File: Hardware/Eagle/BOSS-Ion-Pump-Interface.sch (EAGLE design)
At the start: 38 parts, among them J1 MOLEX-22112022, J2 MOLEX-22112042, J3 MOLEX-22112042, J4 MOLEX-22112062, SW1 SPST-OFFBOARD, SW2 SPST-OFFBOARD, U1 ISO224ADWVR, U2 ISO224ADWVR

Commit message: Re-labeled nets, added 10uF filter on+5V in
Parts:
- added C15: 10uF 50V, AUmlib:C-USC1210
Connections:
- net +15V-BLUE renamed +15V-A
- net +15V-RED renamed +15V-B
- net +VIN-BLUE renamed +VIN-A
- net +VIN-RED renamed +VIN-B
- net FROM-BLUE-PUMP renamed FROM-PUMP-A
- net FROM-RED-PUMP renamed FROM-PUMP-B
- net GND-ISO-BLUE renamed GND-ISO-A
- net GND-ISO-RED renamed GND-ISO-B
- net IN-BLUE renamed IN-A
- net IN-RED renamed IN-B
- net VCAP-BLUE renamed VCAP-A
- net VCAP-RED renamed VCAP-B
- net VDD1-BLUE renamed VDD1-A
- net VDD1-RED renamed VDD1-B
- removed net OUTN-BLUE: J4.5, TVS3.C2, U$11.5, U2.OUTN
- removed net OUTN-RED: J4.4, TVS3.C3, U$11.4, U1.OUTN
- removed net OUTP-BLUE: J4.6, TVS3.C1, U$11.6, U2.OUTP
- removed net OUTP-RED: J4.3, TVS3.C4, U$11.3, U1.OUTP
- new net OUTN-A: J4.5, TVS3.C2, U$11.4, U$11.5, U2.OUTN
- new net OUTN-B: J4.4, TVS3.C3, U1.OUTN
- new net OUTP-A: J4.6, TVS3.C1, U$11.3, U$11.6, U2.OUTP
- new net OUTP-B: J4.3, TVS3.C4, U1.OUTP
- net +5V: now also C15.1
- net GND: now also C15.2
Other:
- moved on the sheet: C4, R2

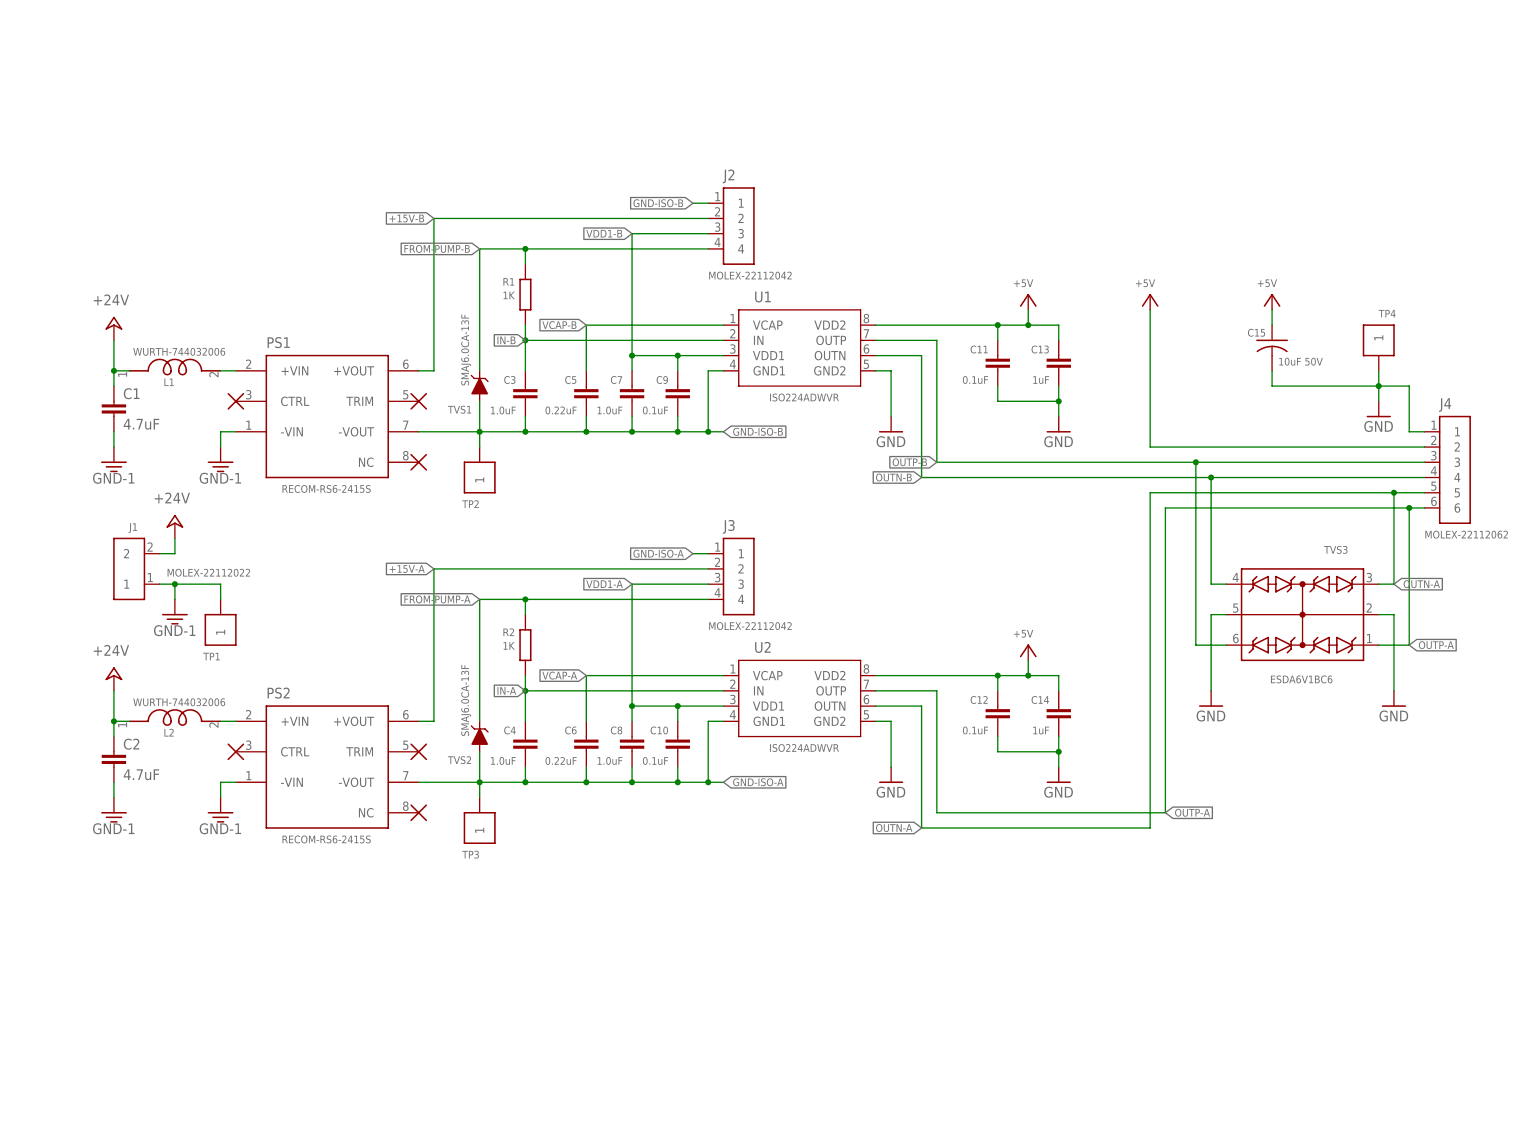
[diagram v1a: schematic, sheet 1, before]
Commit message: Added reverse polarity protection
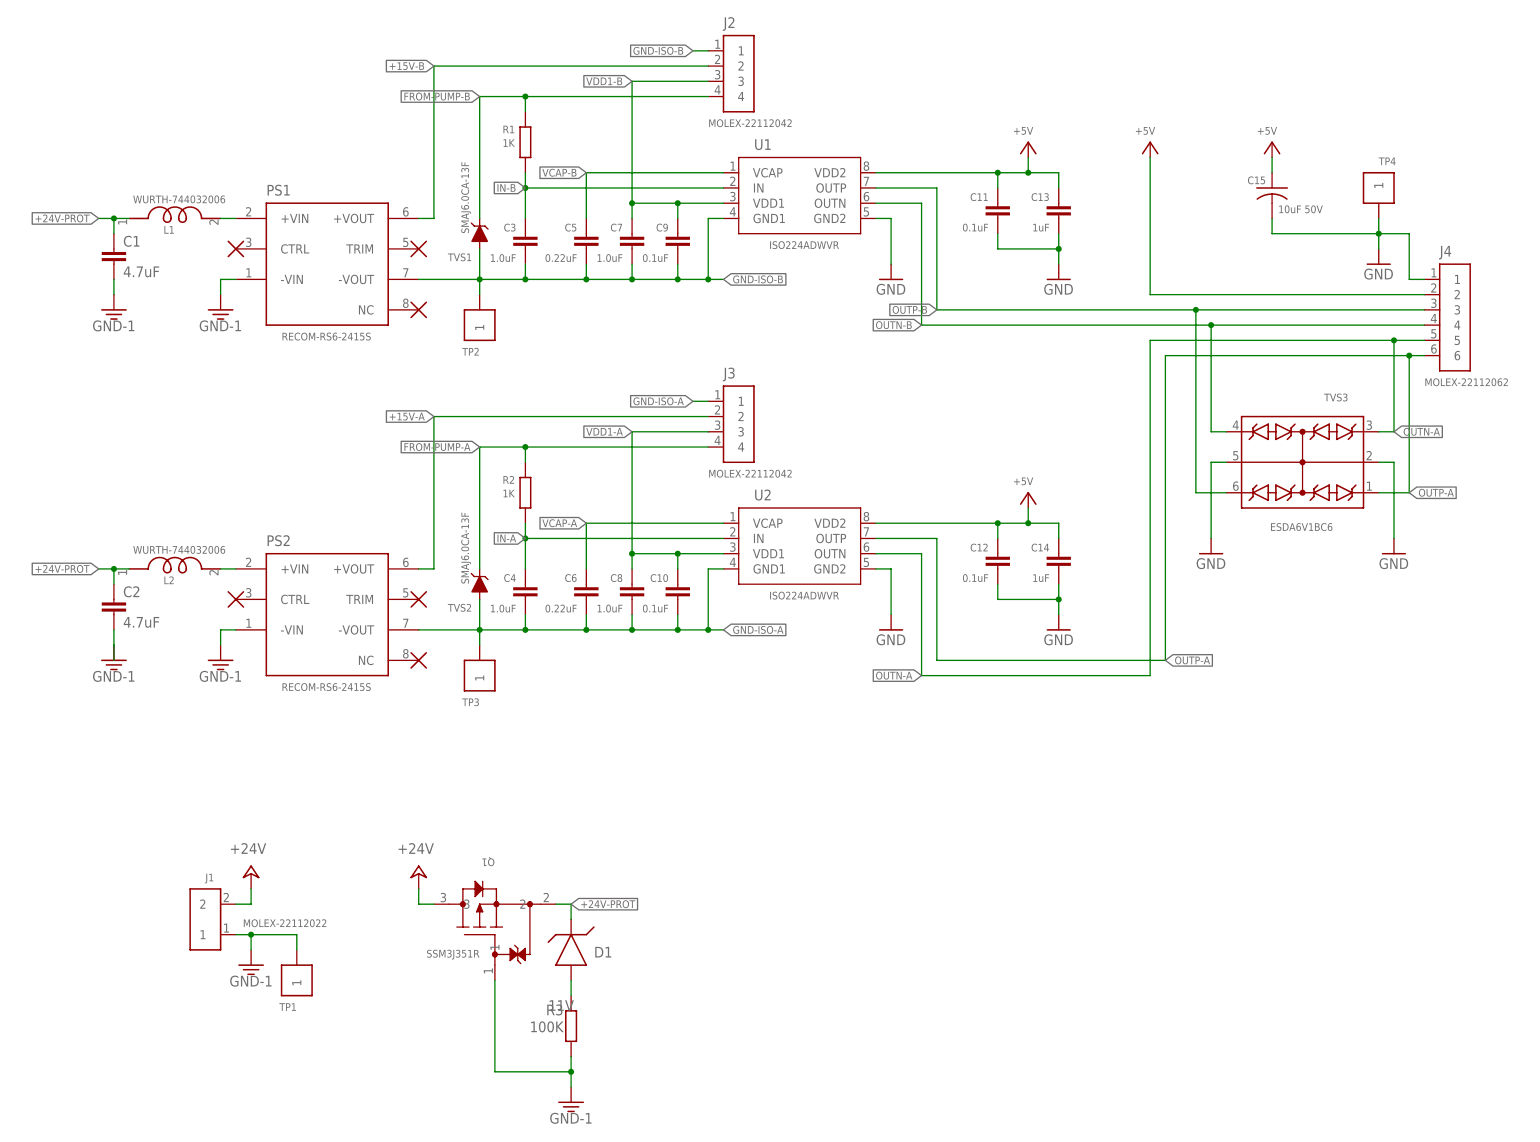
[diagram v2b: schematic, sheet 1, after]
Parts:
- added D1: 11V, AUmlib:ZENER-BZT52C11-7-F
- added Q1: SSM3J351R, AUmlib:P-MOSFET-SSM3J351R
- added R3: 100K, AUmlib:R-EU_R0805
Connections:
- new net +24V-PROT: C1.1, C2.1, D1.C, L1.1, L2.1, Q1.2
- new net N$2: D1.A, R3.2
- net +24V: now also Q1.3; no longer C1.1, C2.1, L1.1, L2.1
- net GND-1: now also Q1.1, R3.1
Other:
- moved on the sheet: C1, C10, C11, C12, C13, C14, C15, C2, C3, C4, C5, C6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

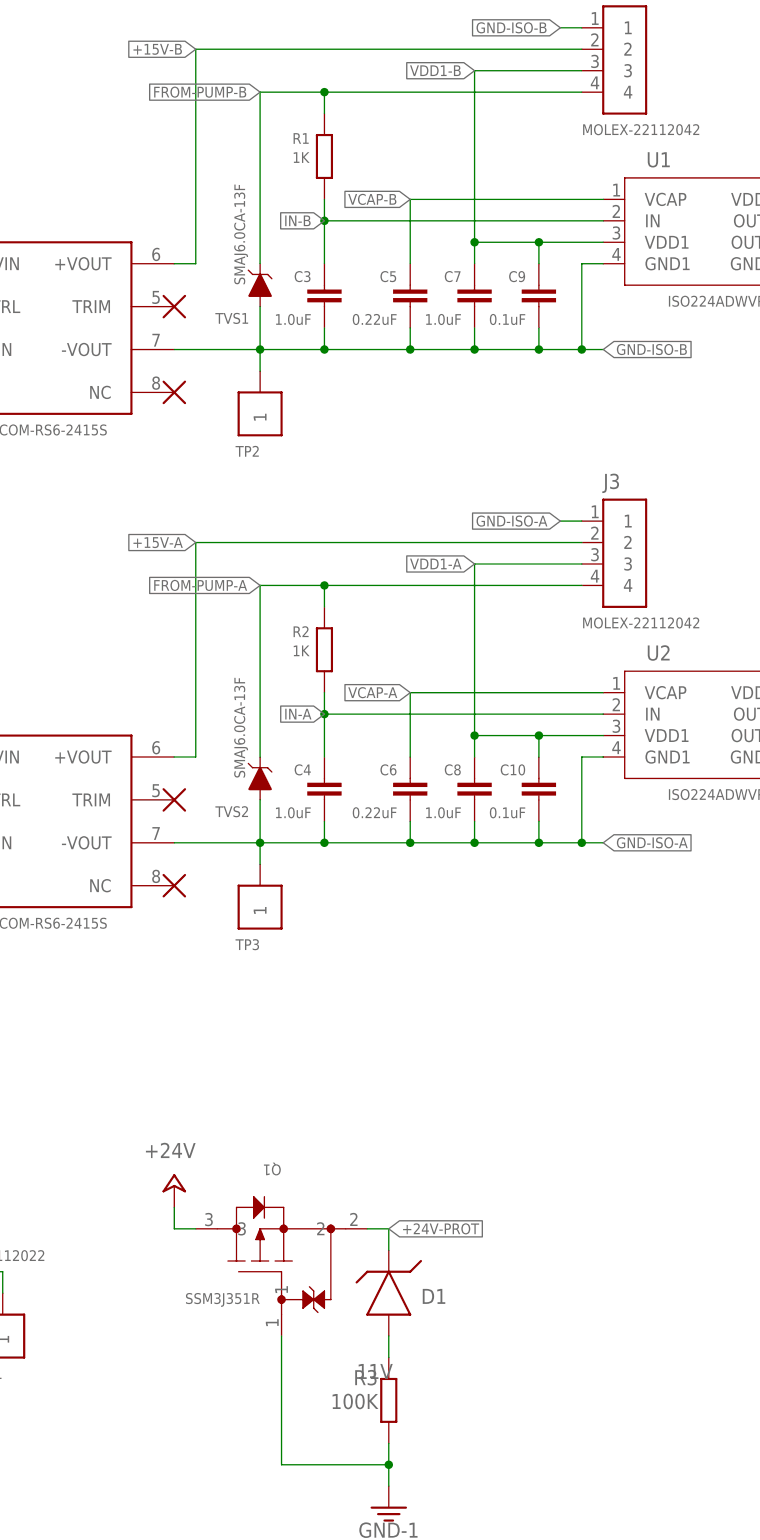
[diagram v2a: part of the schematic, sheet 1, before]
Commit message: Changed TVS diode to 10 V from 6 V and labeled reverse polarity Zener
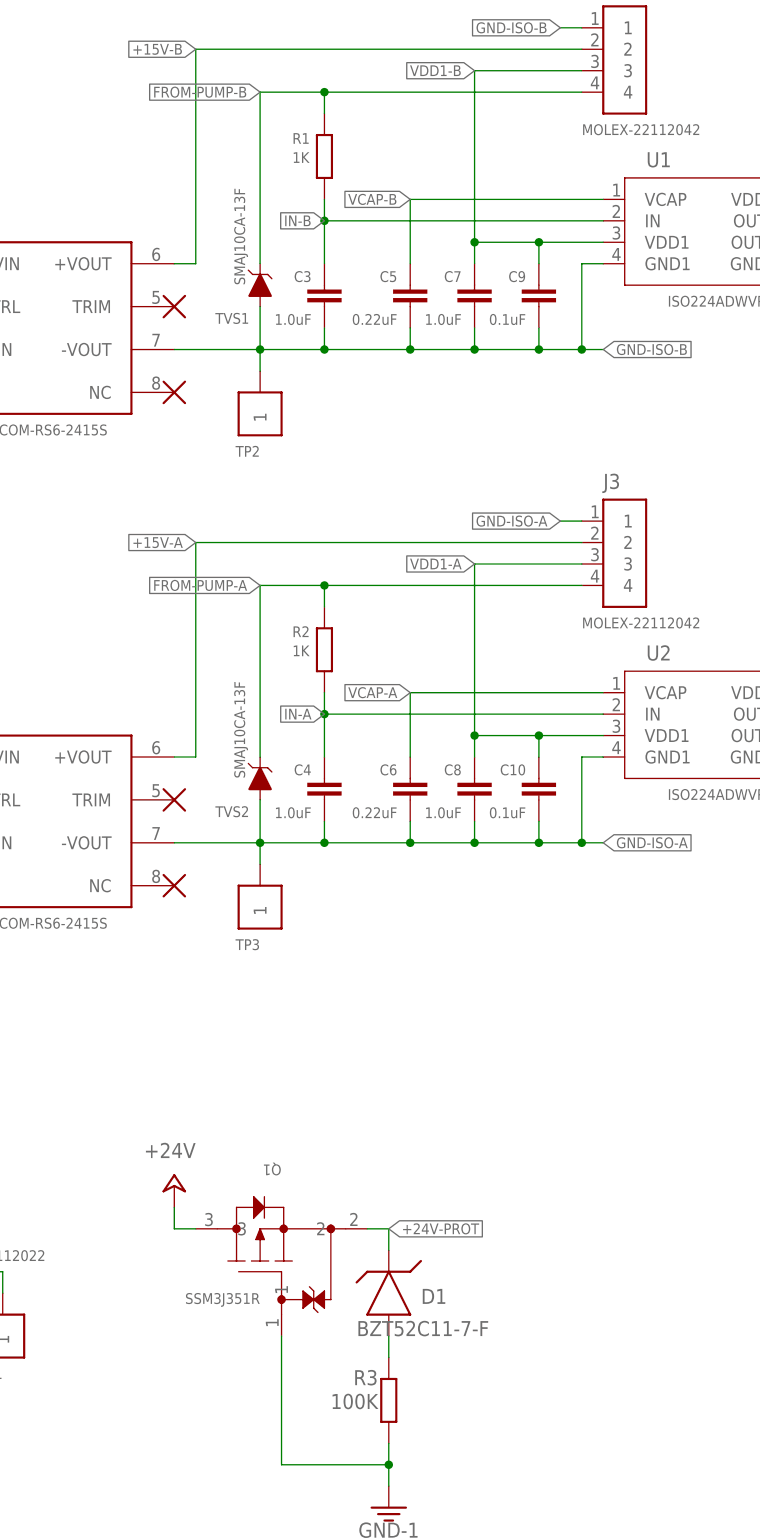
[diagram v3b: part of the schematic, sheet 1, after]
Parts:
- D1: value 11V -> BZT52C11-7-F
- TVS1, TVS2: value SMAJ6.0CA-13F -> SMAJ10CA-13F
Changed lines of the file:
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@@
 <part name="C8" library="AUmlib" library_urn="urn:adsk.eagle:library:9166017" deviceset="C-EU" device="C1206" package3d_urn="urn:adsk.eagle:package:23618/2" value="1.0uF"/>
 <part name="C10" library="AUmlib" library_urn="urn:adsk.eagle:library:9166017" deviceset="C-EU" device="C1206" package3d_urn="urn:adsk.eagle:package:23618/2" value="0.1uF"/>
-<part name="TVS1" library="AUmlib" library_urn="urn:adsk.eagle:library:9166017" deviceset="TVS-DIODE-SMAJ6.0CA-13-F" device="SMA_DIO-M" package3d_urn="urn:adsk.eagle:package:25921539/2" value="SMAJ6.0CA-13F"/>
-<part name="TVS2" library="AUmlib" library_urn="urn:adsk.eagle:library:9166017" deviceset="TVS-DIODE-SMAJ6.0CA-13-F" device="SMA_DIO-M" package3d_urn="urn:adsk.eagle:package:25921539/2" value="SMAJ6.0CA-13F"/>
+<part name="TVS1" library="AUmlib" library_urn="urn:adsk.eagle:library:9166017" deviceset="TVS-DIODE-SMAJ6.0CA-13-F" device="SMA_DIO-M" package3d_urn="urn:adsk.eagle:package:25921539/2" value="SMAJ10CA-13F"/>
+<part name="TVS2" library="AUmlib" library_urn="urn:adsk.eagle:library:9166017" deviceset="TVS-DIODE-SMAJ6.0CA-13-F" device="SMA_DIO-M" package3d_urn="urn:adsk.eagle:package:25921539/2" value="SMAJ10CA-13F"/>
 <part name="TVS3" library="AUmlib" library_urn="urn:adsk.eagle:library:9166017" deviceset="TVS-QUAD-ESDA6V1BC6" device="" package3d_urn="urn:adsk.eagle:package:25920714/2" value="ESDA6V1BC6"/>
 <part name="GND11" library="AUmlib" library_urn="urn:adsk.eagle:library:9166017" deviceset="GND" device=""/>
@@
 <part name="P+6" library="AUmlib" library_urn="urn:adsk.eagle:library:9166017" deviceset="+24V" device=""/>
 <part name="GND13" library="AUmlib" library_urn="urn:adsk.eagle:library:9166017" deviceset="GND-1" device=""/>
-<part name="D1" library="AUmlib" library_urn="urn:adsk.eagle:library:9166017" deviceset="ZENER-BZT52C11-7-F" device="" package3d_urn="urn:adsk.eagle:package:26453057/2" value="11V"/>
+<part name="D1" library="AUmlib" library_urn="urn:adsk.eagle:library:9166017" deviceset="ZENER-BZT52C11-7-F" device="" package3d_urn="urn:adsk.eagle:package:26453057/2" value="BZT52C11-7-F"/>
 </parts>
 <sheets>
@@
 <instance part="D1" gate="A" x="106.68" y="48.26" smashed="yes">
 <attribute name="NAME" x="110.49" y="46.99" size="1.778" layer="95"/>
-<attribute name="VALUE" x="102.87" y="38.1" size="1.778" layer="96"/>
+<attribute name="VALUE" x="102.87" y="43.18" size="1.778" layer="96"/>
 </instance>
 </instances>

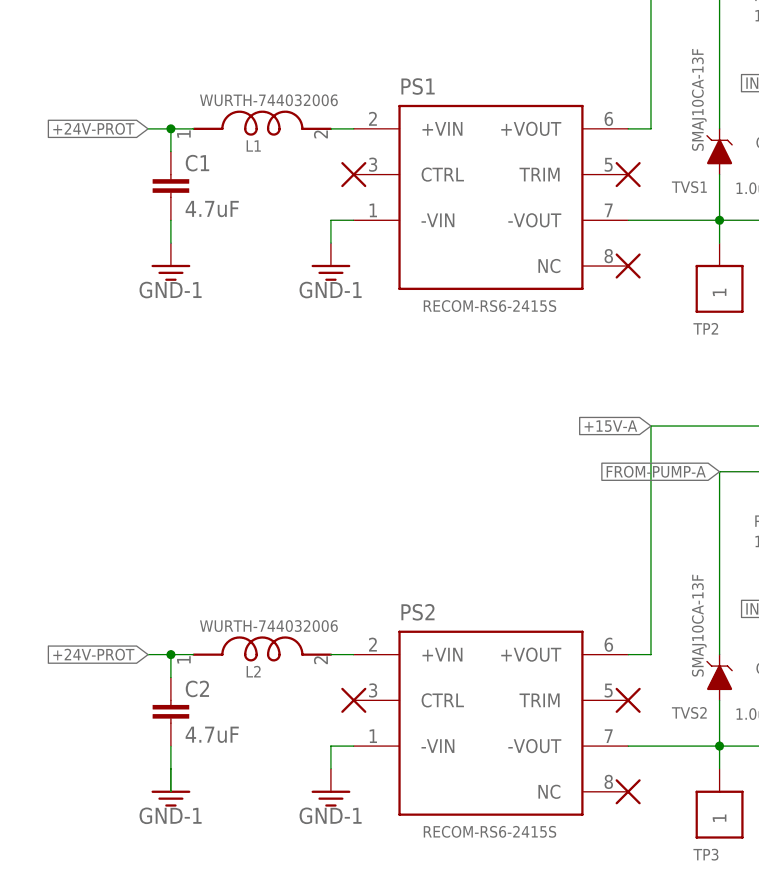
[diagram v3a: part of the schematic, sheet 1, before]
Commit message: Added names to the reverse polarity zener net
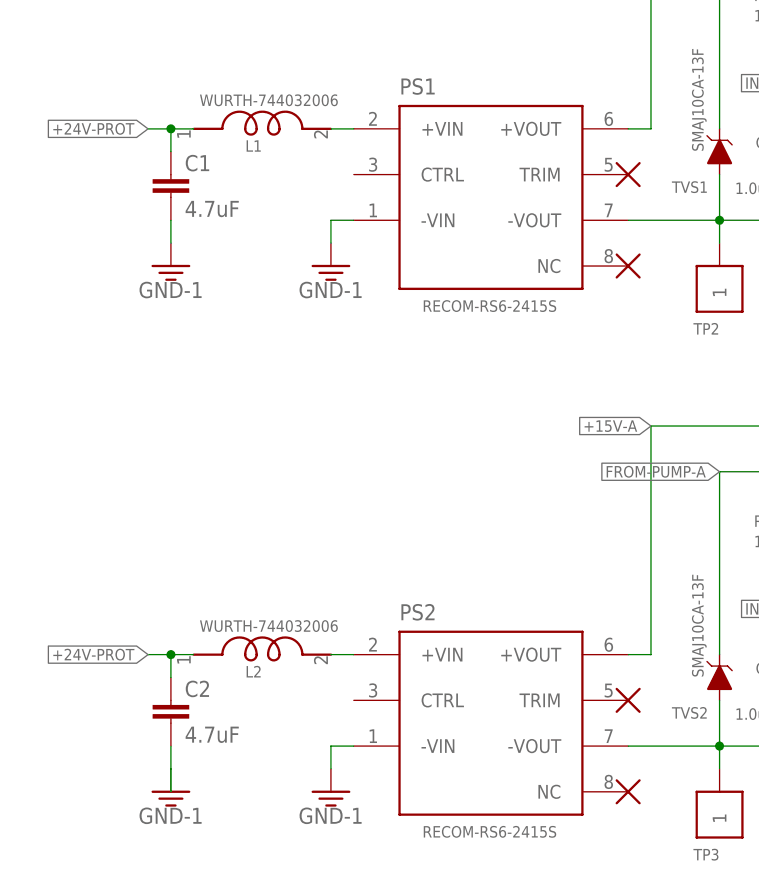
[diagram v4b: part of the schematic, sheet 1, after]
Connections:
- net N$2 renamed REVERSE-POL-ZENER
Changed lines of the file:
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@@
 <setting verticaltext="up"/>
 </settings>
-<grid distance="0.1" unitdist="inch" unit="inch" style="lines" multiple="1" display="no" altdistance="0.01" altunitdist="inch" altunit="inch"/>
+<grid distance="0.1" unitdist="inch" unit="inch" style="lines" multiple="1" display="yes" altdistance="0.01" altunitdist="inch" altunit="inch"/>
 <layers>
 <layer number="1" name="Top" color="4" fill="1" visible="no" active="no"/>
@@
 <part name="TP3" library="AUmlib" library_urn="urn:adsk.eagle:library:9166017" deviceset="TP5000-TESTPOINT-BLK" device="" package3d_urn="urn:adsk.eagle:package:24642442/4"/>
 <part name="TP4" library="AUmlib" library_urn="urn:adsk.eagle:library:9166017" deviceset="TP5000-TESTPOINT-BLK" device="" package3d_urn="urn:adsk.eagle:package:24642442/4"/>
-<part name="U$1" library="AUmlib" library_urn="urn:adsk.eagle:library:9166017" deviceset="NC" device=""/>
 <part name="U$2" library="AUmlib" library_urn="urn:adsk.eagle:library:9166017" deviceset="NC" device=""/>
-<part name="U$3" library="AUmlib" library_urn="urn:adsk.eagle:library:9166017" deviceset="NC" device=""/>
 <part name="U$4" library="AUmlib" library_urn="urn:adsk.eagle:library:9166017" deviceset="NC" device=""/>
 <part name="U$5" library="AUmlib" library_urn="urn:adsk.eagle:library:9166017" deviceset="NC" device=""/>
@@
 <attribute name="NAME" x="241.3" y="179.07" size="1.27" layer="95"/>
 </instance>
-<instance part="U$1" gate="G$1" x="50.8" y="165.1" smashed="yes"/>
 <instance part="U$2" gate="G$1" x="81.28" y="165.1" smashed="yes"/>
-<instance part="U$3" gate="G$1" x="50.8" y="106.68" smashed="yes"/>
 <instance part="U$4" gate="G$1" x="81.28" y="106.68" smashed="yes"/>
 <instance part="U$5" gate="G$1" x="81.28" y="96.52" smashed="yes"/>
@@
 </segment>
 </net>
-<net name="N$2" class="0">
+<net name="REVERSE-POL-ZENER" class="0">
 <segment>
 <pinref part="R3" gate="G$1" pin="2"/>
